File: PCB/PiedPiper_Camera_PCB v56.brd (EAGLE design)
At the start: 48.3 x 66 mm, 24 parts

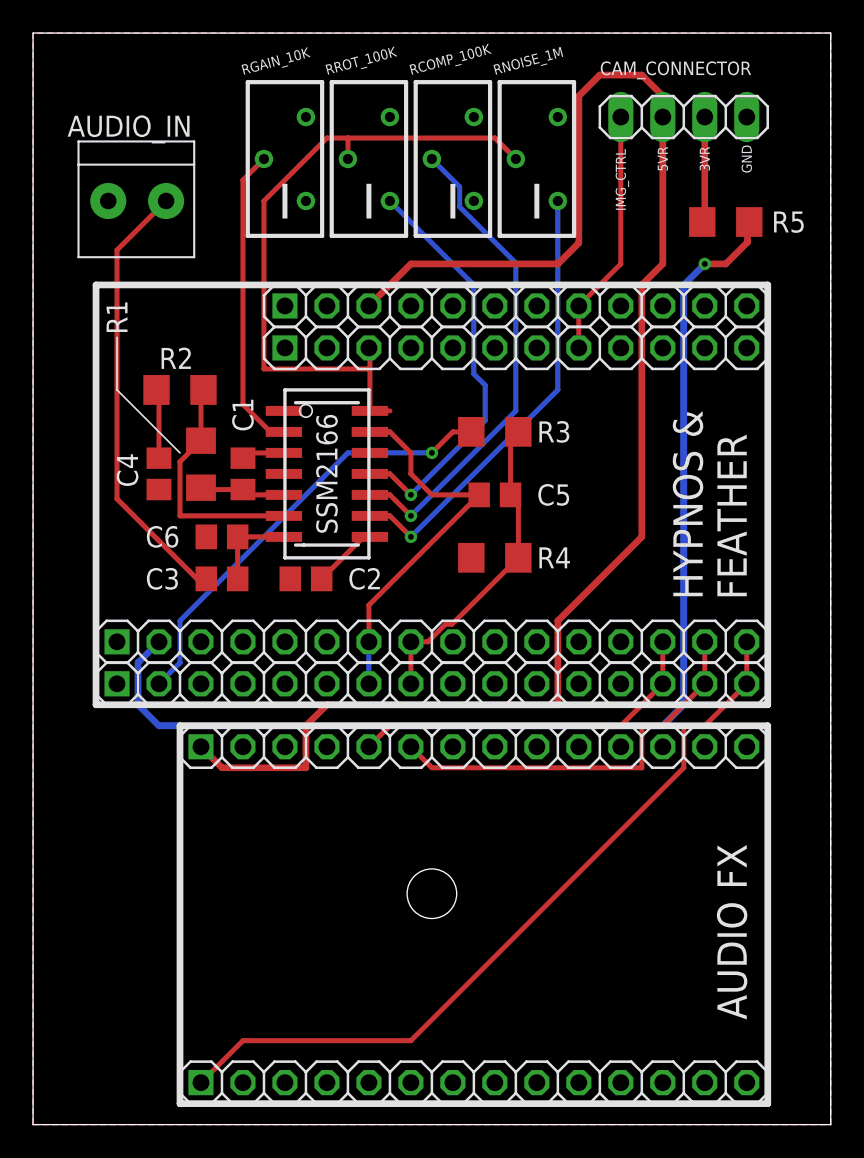
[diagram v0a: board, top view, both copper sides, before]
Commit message: Another PCB revision
Uploaded new PCB revision (in collaboration with Bryson) which includes ground plane vias to reduce capacitance.
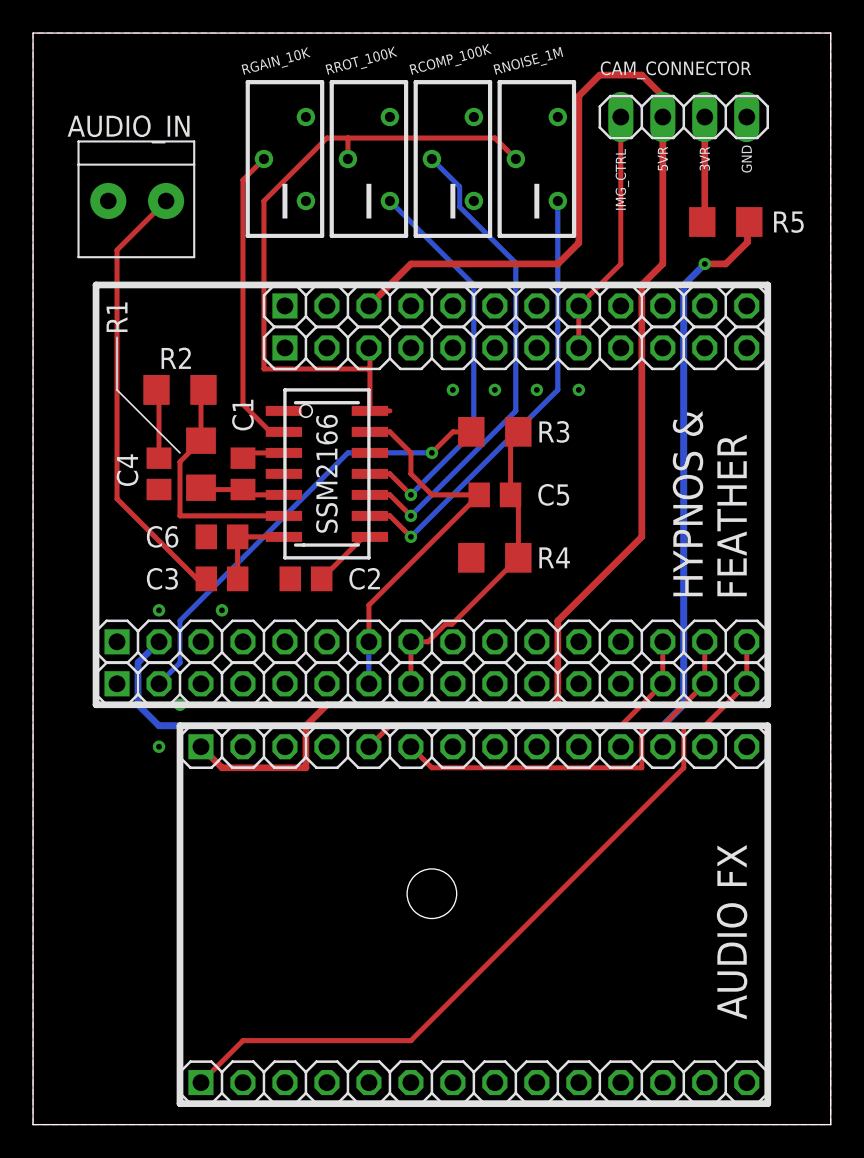
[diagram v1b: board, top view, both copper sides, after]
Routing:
- net ROTATION_POINT_SET: track 25.0 -> 24.5 mm
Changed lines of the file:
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@@
 <class number="0" name="default" width="0" drill="0">
 </class>
+<class number="1" name="gndvia" width="0" drill="0">
+</class>
 </classes>
 <designrules name="default">
@@
 <vertex x="23.666890625" y="40.626446875"/>
 <vertex x="23.726865625" y="40.66791875"/>
-<vertex x="25.718684375" y="42.6597375"/>
-<vertex x="25.763346875" y="42.727159375"/>
-<vertex x="25.7782" y="42.803421875"/>
-<vertex x="25.7782" y="44.522490625"/>
-<vertex x="25.76210625" y="44.601746875"/>
-<vertex x="25.718684375" y="44.666175"/>
-<vertex x="25.0952" y="45.289659375"/>
+<vertex x="25.035684375" y="41.9767375"/>
+<vertex x="25.080346875" y="42.044159375"/>
+<vertex x="25.0952" y="42.120421875"/>
 <vertex x="25.0952" y="46.171475"/>
 <vertex x="25.07910625" y="46.25073125"/>
@@
 </polygonholelist>
 </polygonshape>
+<polygonshape layer="16">
+<polygonoutlineobjects>
+<vertex x="25.993178125" y="41.6819375"/>
+<vertex x="26.051684375" y="41.7227375"/>
+<vertex x="27.575684375" y="43.2467375"/>
+<vertex x="27.620346875" y="43.314159375"/>
+<vertex x="27.6352" y="43.390421875"/>
+<vertex x="27.6352" y="46.171475"/>
+<vertex x="27.61910625" y="46.25073125"/>
+<vertex x="27.573375" y="46.31743125"/>
+<vertex x="27.50525" y="46.3610125"/>
+<vertex x="27.425521875" y="46.374571875"/>
+<vertex x="27.346821875" y="46.355959375"/>
+<vertex x="27.288315625" y="46.315159375"/>
+<vertex x="27.04875625" y="46.0756"/>
+<vertex x="26.29124375" y="46.0756"/>
+<vertex x="26.051684375" y="46.315159375"/>
+<vertex x="25.9842625" y="46.359821875"/>
+<vertex x="25.904759375" y="46.37465"/>
+<vertex x="25.825771875" y="46.35729375"/>
+<vertex x="25.759809375" y="46.31050625"/>
+<vertex x="25.71731875" y="46.24169375"/>
+<vertex x="25.7048" y="46.171475"/>
+<vertex x="25.7048" y="41.866421875"/>
+<vertex x="25.72089375" y="41.787165625"/>
+<vertex x="25.766625" y="41.720465625"/>
+<vertex x="25.83475" y="41.676884375"/>
+<vertex x="25.914478125" y="41.663325"/>
+</polygonoutlineobjects>
+<polygonoutlinesegments>
+<vertex x="25.993178125" y="41.6819375"/>
+<vertex x="26.051684375" y="41.7227375"/>
+<vertex x="27.575684375" y="43.2467375"/>
+<vertex x="27.620346875" y="43.314159375"/>
+<vertex x="27.6352" y="43.390421875"/>
+<vertex x="27.6352" y="46.171475"/>
+<vertex x="27.61910625" y="46.25073125"/>
+<vertex x="27.573375" y="46.31743125"/>
+<vertex x="27.50525" y="46.3610125"/>
+<vertex x="27.425521875" y="46.374571875"/>
+<vertex x="27.346821875" y="46.355959375"/>
+<vertex x="27.288315625" y="46.315159375"/>
+<vertex x="27.04875625" y="46.0756"/>
+<vertex x="26.29124375" y="46.0756"/>
+<vertex x="26.051684375" y="46.315159375"/>
+<vertex x="25.9842625" y="46.359821875"/>
+<vertex x="25.904759375" y="46.37465"/>
+<vertex x="25.825771875" y="46.35729375"/>
+<vertex x="25.759809375" y="46.31050625"/>
+<vertex x="25.71731875" y="46.24169375"/>
+<vertex x="25.7048" y="46.171475"/>
+<vertex x="25.7048" y="41.866421875"/>
+<vertex x="25.72089375" y="41.787165625"/>
+<vertex x="25.766625" y="41.720465625"/>
+<vertex x="25.83475" y="41.676884375"/>
+<vertex x="25.914478125" y="41.663325"/>
+<vertex x="25.993178125" y="41.6819375"/>
+</polygonoutlinesegments>
+</polygonshape>
+<polygonshape layer="16">
+<polygonoutlineobjects>
+<vertex x="28.533178125" y="42.9519375"/>
+<vertex x="28.591684375" y="42.9927375"/>
+<vertex x="30.115684375" y="44.5167375"/>
+<vertex x="30.160346875" y="44.584159375"/>
+<vertex x="30.1752" y="44.660421875"/>
+<vertex x="30.1752" y="46.171475"/>
+<vertex x="30.15910625" y="46.25073125"/>
+<vertex x="30.113375" y="46.31743125"/>
+<vertex x="30.04525" y="46.3610125"/>
+<vertex x="29.965521875" y="46.374571875"/>
+<vertex x="29.886821875" y="46.355959375"/>
+<vertex x="29.828315625" y="46.315159375"/>
+<vertex x="29.58875625" y="46.0756"/>
+<vertex x="28.83124375" y="46.0756"/>
+<vertex x="28.591684375" y="46.315159375"/>
+<vertex x="28.5242625" y="46.359821875"/>
+<vertex x="28.444759375" y="46.37465"/>
+<vertex x="28.365771875" y="46.35729375"/>
+<vertex x="28.299809375" y="46.31050625"/>
+<vertex x="28.25731875" y="46.24169375"/>
+<vertex x="28.2448" y="46.171475"/>
+<vertex x="28.2448" y="43.136421875"/>
+<vertex x="28.26089375" y="43.057165625"/>
+<vertex x="28.306625" y="42.990465625"/>
+<vertex x="28.37475" y="42.946884375"/>
+<vertex x="28.454478125" y="42.933325"/>
+</polygonoutlineobjects>
+<polygonoutlinesegments>
+<vertex x="28.533178125" y="42.9519375"/>
+<vertex x="28.591684375" y="42.9927375"/>
+<vertex x="30.115684375" y="44.5167375"/>
+<vertex x="30.160346875" y="44.584159375"/>
+<vertex x="30.1752" y="44.660421875"/>
+<vertex x="30.1752" y="46.171475"/>
+<vertex x="30.15910625" y="46.25073125"/>
+<vertex x="30.113375" y="46.31743125"/>
+<vertex x="30.04525" y="46.3610125"/>
+<vertex x="29.965521875" y="46.374571875"/>
+<vertex x="29.886821875" y="46.355959375"/>
+<vertex x="29.828315625" y="46.315159375"/>
+<vertex x="29.58875625" y="46.0756"/>
+<vertex x="28.83124375" y="46.0756"/>
+<vertex x="28.591684375" y="46.315159375"/>
+<vertex x="28.5242625" y="46.359821875"/>
+<vertex x="28.444759375" y="46.37465"/>
+<vertex x="28.365771875" y="46.35729375"/>
+<vertex x="28.299809375" y="46.31050625"/>
+<vertex x="28.25731875" y="46.24169375"/>
+<vertex x="28.2448" y="46.171475"/>
+<vertex x="28.2448" y="43.136421875"/>
+<vertex x="28.26089375" y="43.057165625"/>
+<vertex x="28.306625" y="42.990465625"/>
+<vertex x="28.37475" y="42.946884375"/>
+<vertex x="28.454478125" y="42.933325"/>
+<vertex x="28.533178125" y="42.9519375"/>
+</polygonoutlinesegments>
+</polygonshape>
 </polygonfilldetails>
 </polygonpour>
+<via x="31.75" y="44.45" extent="1-16" drill="0.35"/>
+<via x="29.21" y="44.45" extent="1-16" drill="0.35"/>
+<via x="26.67" y="44.45" extent="1-16" drill="0.35"/>
+<via x="24.13" y="44.45" extent="1-16" drill="0.35"/>
+<via x="7.62" y="25.4" extent="1-16" drill="0.35"/>
+<via x="6.35" y="22.86" extent="1-16" drill="0.35"/>
+<via x="10.16" y="31.115" extent="1-16" drill="0.35"/>
+<via x="6.35" y="31.115" extent="1-16" drill="0.35"/>
 </signal>
 <signal name="A2">
@@
 <wire x1="35.56" y1="63.5" x2="36.83" y2="62.23" width="0.4064" layer="1"/>
 <wire x1="36.83" y1="62.23" x2="36.83" y2="60.96" width="0.4064" layer="1"/>
-<wire x1="35.56" y1="35.56" x2="35.56" y2="50.8" width="0.4064" layer="1"/>
+<wire x1="35.56" y1="50.8" x2="35.56" y2="35.56" width="0.4064" layer="1"/>
 <wire x1="35.56" y1="35.56" x2="30.48" y2="30.48" width="0.4064" layer="1"/>
 <wire x1="30.48" y1="30.48" x2="30.48" y2="25.4" width="0.4064" layer="1"/>
@@
 <wire x1="15.24" y1="21.59" x2="10.16" y2="21.59" width="0.4064" layer="1"/>
 <wire x1="10.16" y1="21.59" x2="8.89" y2="22.86" width="0.4064" layer="1"/>
-<wire x1="35.56" y1="50.8" x2="36.83" y2="52.07" width="0.4064" layer="1"/>
+<wire x1="36.83" y1="52.07" x2="35.56" y2="50.8" width="0.4064" layer="1"/>
 <wire x1="36.83" y1="60.96" x2="36.83" y2="52.07" width="0.4064" layer="1"/>
 </signal>
@@
 <wire x1="19.11" y1="39.37" x2="20.32" y2="39.37" width="0.3048" layer="1"/>
 <wire x1="20.32" y1="55.88" x2="25.4" y2="50.8" width="0.3048" layer="16"/>
-<wire x1="25.4" y1="50.8" x2="25.4" y2="45.4159125" width="0.3048" layer="16"/>
-<wire x1="25.4" y1="45.4159125" x2="26.083" y2="44.7329125" width="0.3048" layer="16"/>
-<wire x1="26.083" y1="44.7329125" x2="26.083" y2="42.593" width="0.3048" layer="16"/>
-<wire x1="26.083" y1="42.593" x2="21.59" y2="38.1" width="0.3048" layer="16"/>
+<wire x1="25.4" y1="41.91" x2="21.59" y2="38.1" width="0.3048" layer="16"/>
+<wire x1="25.4" y1="50.8" x2="25.4" y2="41.91" width="0.3048" layer="16"/>
 </signal>
 <signal name="N$1">
